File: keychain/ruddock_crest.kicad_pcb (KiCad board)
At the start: 2 copper layers, 76.1 x 83.8 mm, 3 parts

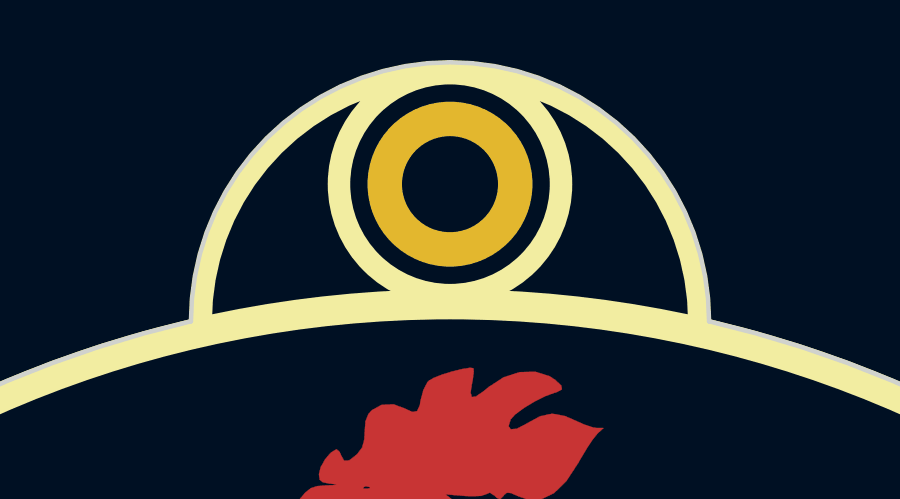
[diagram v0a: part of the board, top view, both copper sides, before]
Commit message: Enlarge hole to 4.5mm
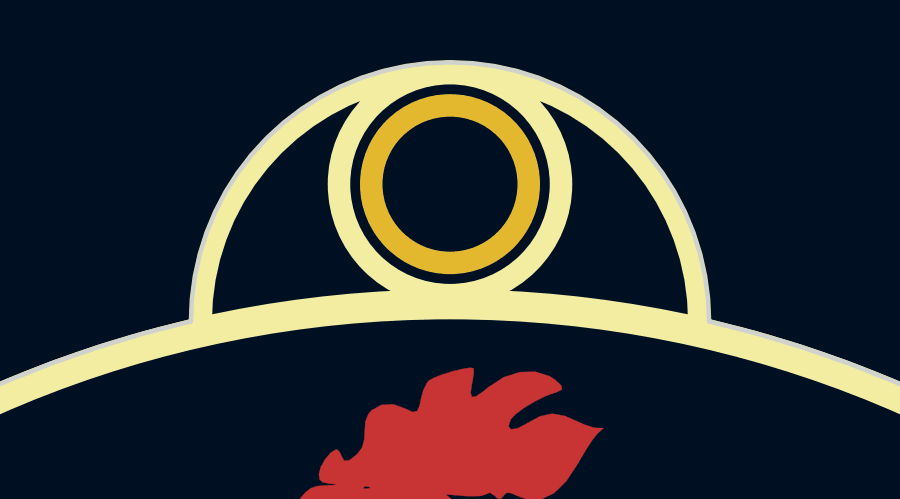
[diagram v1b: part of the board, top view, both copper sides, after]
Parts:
- REF**: value MountingHole_3.2mm_M3_ISO14580_Pad -> MountingHole
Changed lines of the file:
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@@
     (mod_text_size 1 1)
     (mod_text_width 0.15)
-    (pad_size 4.8 4.8)
-    (pad_drill 3.2)
+    (pad_size 6 6)
+    (pad_drill 4.5)
     (pad_to_mask_clearance 0.2)
     (solder_mask_min_width 0.25)
@@
       (effects (font (size 1 1) (thickness 0.15)))
     )
-    (fp_text value MountingHole_3.2mm_M3_ISO14580_Pad (at 0 3.75) (layer F.Fab)
+    (fp_text value MountingHole (at 0 3.75) (layer F.Fab)
       (effects (font (size 1 1) (thickness 0.15)))
     )
@@
       (effects (font (size 1 1) (thickness 0.15)))
     )
-    (pad 1 thru_hole circle (at 0 0) (size 5.5 5.5) (drill 3.2) (layers *.Cu *.Mask))
+    (pad 1 thru_hole circle (at 0 0) (size 6 6) (drill 4.5) (layers *.Cu *.Mask))
   )
   (module crest:ruddock_mask_small (layer F.Cu)
